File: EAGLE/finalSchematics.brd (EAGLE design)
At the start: 100 x 80 mm, 8 parts, among them IC1 STM32F103RBT, Q1 8MHz 131-220

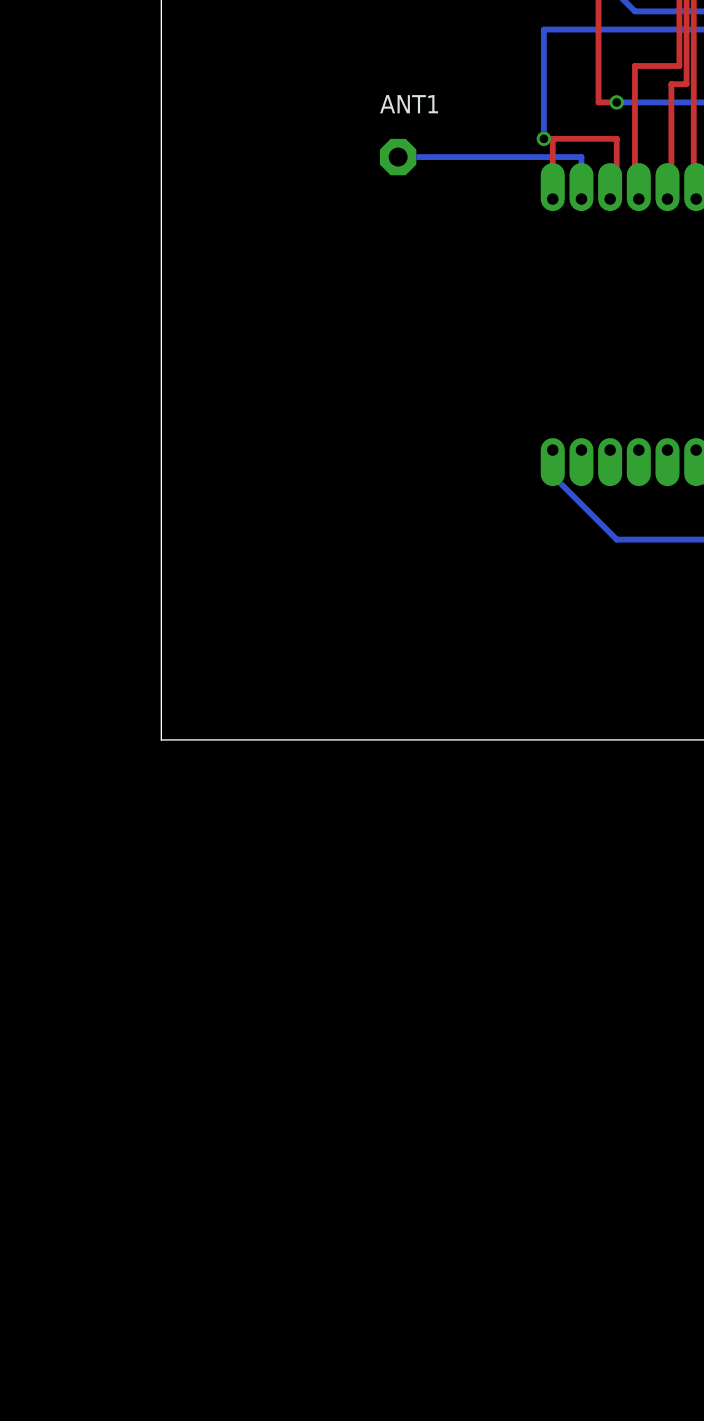
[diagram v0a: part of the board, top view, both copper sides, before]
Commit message: Eagle file ready for meeting with Vojta S.
Missing GPS module footer. Our module is L70 and only L80 library was
found. Will have to resolve later by creating a library at Mucirna.

Repositories folder updated with new documentation
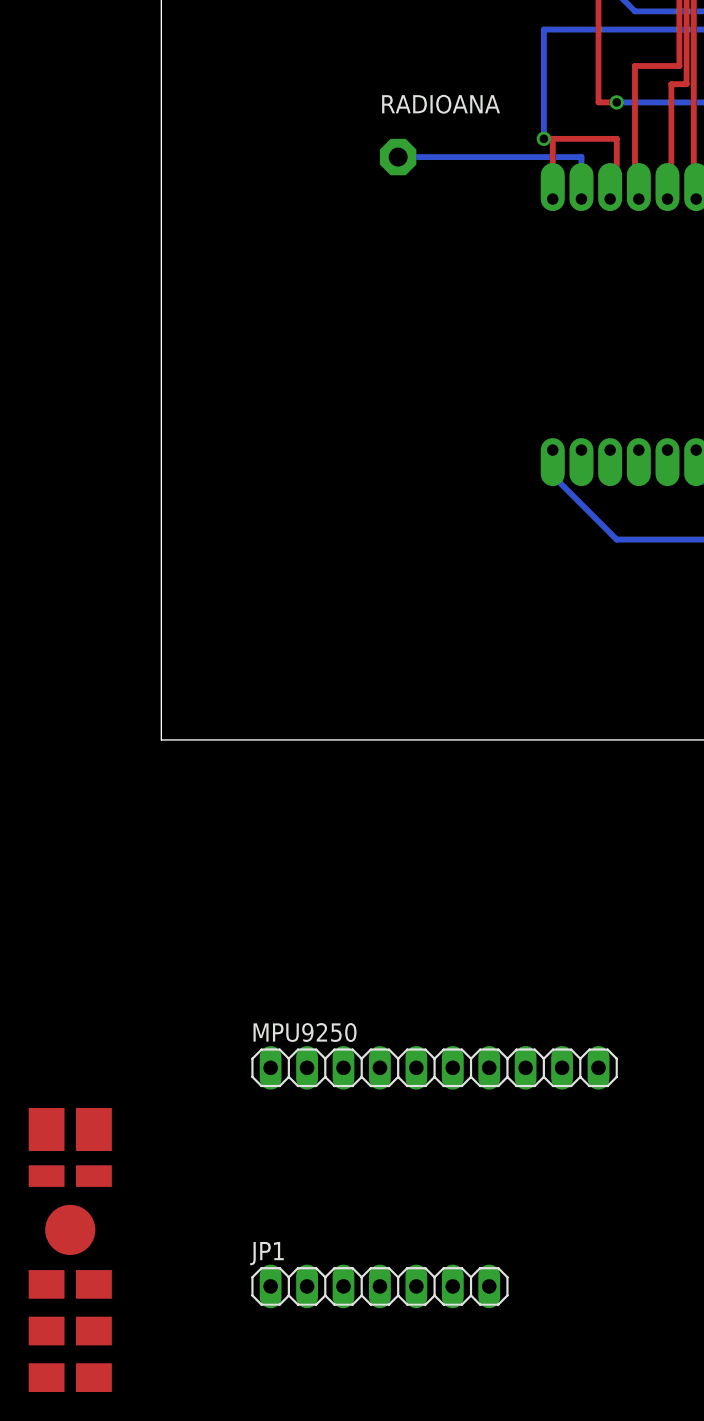
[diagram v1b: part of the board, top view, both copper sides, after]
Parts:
- added GPSANA: ANT-NSG4712-6, roundsolutions:ANT-NSG4712-6
- added JP1: (no value), pinhead:1X07
- added MPU9250: (no value), pinhead:1X10
- renumbered ANT1 to RADIOANA, BPM180 to BME280
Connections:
- new net ADO: MPU9250.4
- new net CD1: JP1.7
- new net CS: JP1.1
- new net DI: JP1.2
- new net DO: JP1.6
- new net ECL: MPU9250.5
- new net EDA: MPU9250.6
- new net FSYNC: MPU9250.1
- new net INT: MPU9250.3
- new net NCS: MPU9250.2
- new net SCK: JP1.4
- new net SCL: MPU9250.8
- new net SDA: MPU9250.7
- new net VCC: JP1.3, MPU9250.10
- net GND: now also JP1.5, MPU9250.9
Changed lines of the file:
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@@
 <layers>
 <layer number="1" name="Top" color="4" fill="1" visible="yes" active="yes"/>
+<layer number="2" name="Route2" color="1" fill="3" visible="no" active="no"/>
+<layer number="3" name="Route3" color="4" fill="3" visible="no" active="no"/>
+<layer number="4" name="Route4" color="1" fill="4" visible="no" active="no"/>
+<layer number="5" name="Route5" color="4" fill="4" visible="no" active="no"/>
+<layer number="6" name="Route6" color="1" fill="8" visible="no" active="no"/>
+<layer number="7" name="Route7" color="4" fill="8" visible="no" active="no"/>
+<layer number="8" name="Route8" color="1" fill="2" visible="no" active="no"/>
+<layer number="9" name="Route9" color="4" fill="2" visible="no" active="no"/>
+<layer number="10" name="Route10" color="1" fill="7" visible="no" active="no"/>
+<layer number="11" name="Route11" color="4" fill="7" visible="no" active="no"/>
+<layer number="12" name="Route12" color="1" fill="5" visible="no" active="no"/>
+<layer number="13" name="Route13" color="4" fill="5" visible="no" active="no"/>
+<layer number="14" name="Route14" color="1" fill="6" visible="no" active="no"/>
+<layer number="15" name="Route15" color="4" fill="6" visible="no" active="no"/>
 <layer number="16" name="Bottom" color="1" fill="1" visible="yes" active="yes"/>
 <layer number="17" name="Pads" color="2" fill="1" visible="yes" active="yes"/>
@@
 </autorouter>
 <elements>
-<element name="ANT1" library="discrete" package="PAD-01" value="" x="16.51" y="40.64"/>
+<element name="RADIOANA" library="discrete" package="PAD-01" value="" x="16.51" y="40.64"/>
 <element name="C1" library="rcl" package="C0805" value="4.7p 906-099" x="54.61" y="69.85" rot="R180"/>
 <element name="C2" library="rcl" package="C0805" value="4.7p 906-099" x="39.37" y="76.2" rot="R180"/>
@@
 <element name="R1" library="rcl" package="R0805" value="10k 901-655" x="50.8" y="59.69" rot="R180"/>
 <element name="U$1" library="RFM69mod" package="20X16BOARD" value="RFM69" x="34.29" y="29.21" rot="MR90"/>
-<element name="BPM180" library="pinhead" package="1X05/90" value="" x="76.2" y="62.23" rot="MR90"/>
+<element name="BME280" library="pinhead" package="1X05/90" value="" x="76.2" y="62.23" rot="MR90"/>
+<element name="MPU9250" library="pinhead" package="1X10" value="" x="19.05" y="-22.86"/>
+<element name="JP1" library="pinhead" package="1X07" value="" x="15.24" y="-38.1"/>
+<element name="GPSANA" library="roundsolutions" package="ANT-NSG4712-6" value="ANT-NSG4712-6" x="-6.35" y="-35.56"/>
 </elements>
 <signals>
@@
 <wire x1="26.67" y1="49.53" x2="26.67" y2="41.91" width="0.4064" layer="16"/>
 <via x="26.67" y="41.91" extent="1-16" drill="0.6"/>
-<contactref element="BPM180" pad="3"/>
+<contactref element="BME280" pad="3"/>
 <via x="52.07" y="49.53" extent="1-16" drill="0.6" shape="square"/>
 <wire x1="52.07" y1="58.42" x2="51.75" y2="59.69" width="0.4064" layer="1"/>
@@
 <wire x1="40.32" y1="76.2" x2="52.07" y2="76.2" width="0.4064" layer="1"/>
 <wire x1="52.07" y1="76.2" x2="58.42" y2="69.85" width="0.4064" layer="1"/>
+<contactref element="MPU9250" pad="9"/>
+<contactref element="JP1" pad="5"/>
+<wire x1="27.94" y1="-22.86" x2="27.29" y2="37.71" width="0" layer="19" extent="1-1"/>
+<wire x1="17.78" y1="-38.1" x2="27.94" y2="-22.86" width="0" layer="19" extent="1-1"/>
 </signal>
 <signal name="NC">
@@
 <signal name="N$3">
 <contactref element="U$1" pad="ANA"/>
-<contactref element="ANT1" pad="1"/>
+<contactref element="RADIOANA" pad="1"/>
 <wire x1="16.51" y1="40.64" x2="29.29" y2="40.64" width="0.4064" layer="16"/>
 <wire x1="29.29" y1="40.64" x2="29.29" y2="37.71" width="0.4064" layer="16"/>
@@
 <signal name="+3V3">
 <contactref element="U$1" pad="3.3V"/>
-<contactref element="BPM180" pad="2"/>
+<contactref element="BME280" pad="2"/>
 <wire x1="72.39" y1="59.69" x2="66.04" y2="59.69" width="0.4064" layer="16"/>
 <wire x1="66.04" y1="59.69" x2="58.42" y2="52.07" width="0.4064" layer="16"/>
@@
 <signal name="SCL_BPM180">
 <contactref element="IC1" pad="61"/>
-<contactref element="BPM180" pad="4"/>
+<contactref element="BME280" pad="4"/>
 <wire x1="45.12" y1="61.94" x2="53.05" y2="61.94" width="0.4064" layer="1"/>
 <wire x1="53.05" y1="61.94" x2="53.34" y2="62.23" width="0.4064" layer="1"/>
@@
 <signal name="SDA_BPM180">
 <contactref element="IC1" pad="62"/>
-<contactref element="BPM180" pad="5"/>
+<contactref element="BME280" pad="5"/>
 <wire x1="45.12" y1="62.44" x2="48.47" y2="62.44" width="0.4064" layer="1"/>
 <wire x1="48.47" y1="62.44" x2="49.53" y2="63.5" width="0.4064" layer="1"/>
@@
 <wire x1="53.34" y1="67.31" x2="72.39" y2="67.31" width="0.4064" layer="16"/>
 </signal>
+<signal name="VCC">
+<contactref element="MPU9250" pad="10"/>
+<contactref element="JP1" pad="3"/>
+<wire x1="30.48" y1="-22.86" x2="12.7" y2="-38.1" width="0" layer="19" extent="1-1"/>
+</signal>
+<signal name="SCL">
+<contactref element="MPU9250" pad="8"/>
+</signal>
+<signal name="SDA">
+<contactref element="MPU9250" pad="7"/>
+</signal>
+<signal name="EDA">
+<contactref element="MPU9250" pad="6"/>
+</signal>
+<signal name="ECL">
+<contactref element="MPU9250" pad="5"/>
+</signal>
+<signal name="ADO">
+<contactref element="MPU9250" pad="4"/>
+</signal>
+<signal name="INT">
+<contactref element="MPU9250" pad="3"/>
+</signal>
+<signal name="NCS">
+<contactref element="MPU9250" pad="2"/>
+</signal>
+<signal name="FSYNC">
+<contactref element="MPU9250" pad="1"/>
+</signal>
+<signal name="CS">
+<contactref element="JP1" pad="1"/>
+</signal>
+<signal name="DI">
+<contactref element="JP1" pad="2"/>
+</signal>
+<signal name="SCK">
+<contactref element="JP1" pad="4"/>
+</signal>
+<signal name="DO">
+<contactref element="JP1" pad="6"/>
+</signal>
+<signal name="CD1">
+<contactref element="JP1" pad="7"/>
+</signal>
 </signals>

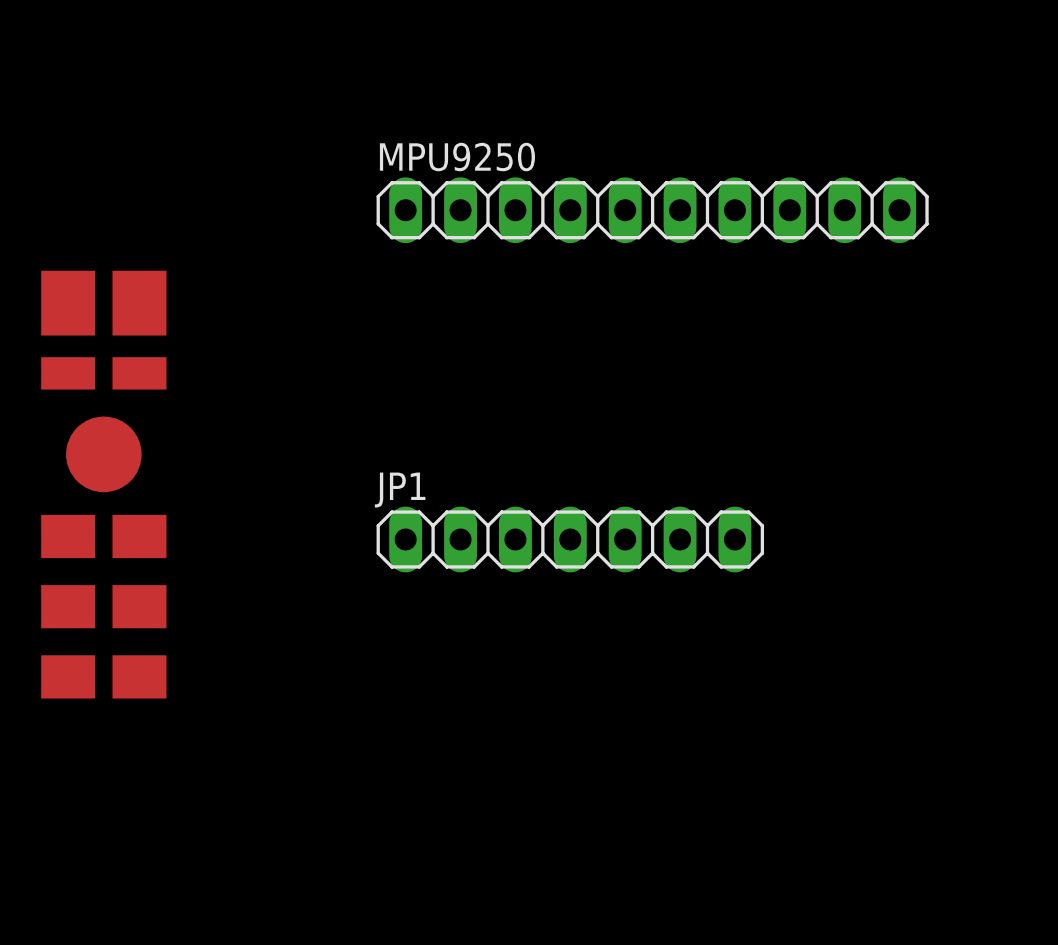
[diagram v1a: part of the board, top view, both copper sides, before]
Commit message: SDfixed, Gyro fixed
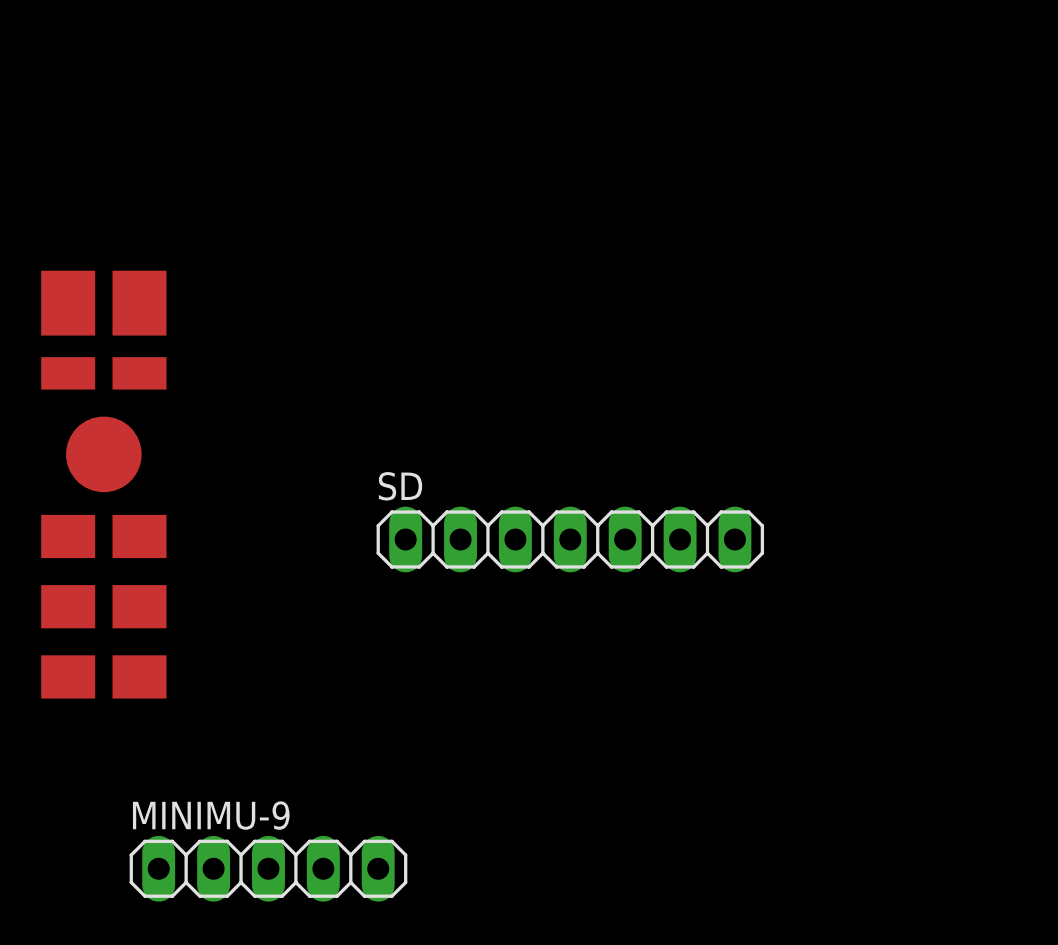
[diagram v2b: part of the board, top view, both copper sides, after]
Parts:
- removed MPU9250: (no value), pinhead:1X10
- added MINIMU-9: (no value), pinhead:1X05
- renumbered JP1 to SD
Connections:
- removed net ADO: MPU9250.4
- removed net ECL: MPU9250.5
- removed net EDA: MPU9250.6
- removed net FSYNC: MPU9250.1
- removed net INT: MPU9250.3
- removed net NCS: MPU9250.2
- new net VIN: MINIMU-9.2
- net GND: now also MINIMU-9.3; no longer MPU9250.9
- net SCL: now also MINIMU-9.5; no longer MPU9250.8
- net SDA: now also MINIMU-9.4; no longer MPU9250.7
- net VCC: no longer MPU9250.10
- net VDD: now also MINIMU-9.1
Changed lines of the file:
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@@
 <element name="U$1" library="RFM69mod" package="20X16BOARD" value="RFM69" x="34.29" y="29.21" rot="MR90"/>
 <element name="BME280" library="pinhead" package="1X05/90" value="" x="76.2" y="62.23" rot="MR90"/>
-<element name="MPU9250" library="pinhead" package="1X10" value="" x="19.05" y="-22.86"/>
-<element name="JP1" library="pinhead" package="1X07" value="" x="15.24" y="-38.1"/>
+<element name="SD" library="pinhead" package="1X07" value="" x="15.24" y="-38.1"/>
 <element name="GPSANA" library="roundsolutions" package="ANT-NSG4712-6" value="ANT-NSG4712-6" x="-6.35" y="-35.56"/>
+<element name="MINIMU-9" library="pinhead" package="1X05" value="" x="1.27" y="-53.34"/>
 </elements>
 <signals>
@@
 <wire x1="33.08" y1="55.94" x2="31.75" y2="54.61" width="0.4064" layer="1"/>
 <via x="31.75" y="54.61" extent="1-16" drill="0.6"/>
+<contactref element="MINIMU-9" pad="1"/>
+<wire x1="-3.81" y1="-53.34" x2="33.02" y2="50.8" width="0" layer="19" extent="16-16"/>
 </signal>
 <signal name="VSS">
@@
 <wire x1="40.32" y1="76.2" x2="52.07" y2="76.2" width="0.4064" layer="1"/>
 <wire x1="52.07" y1="76.2" x2="58.42" y2="69.85" width="0.4064" layer="1"/>
-<contactref element="MPU9250" pad="9"/>
-<contactref element="JP1" pad="5"/>
-<wire x1="27.94" y1="-22.86" x2="27.29" y2="37.71" width="0" layer="19" extent="1-1"/>
-<wire x1="17.78" y1="-38.1" x2="27.94" y2="-22.86" width="0" layer="19" extent="1-1"/>
+<contactref element="SD" pad="5"/>
+<contactref element="MINIMU-9" pad="3"/>
+<wire x1="17.78" y1="-38.1" x2="27.29" y2="37.71" width="0" layer="19" extent="1-1"/>
+<wire x1="1.27" y1="-53.34" x2="17.78" y2="-38.1" width="0" layer="19" extent="1-1"/>
 </signal>
 <signal name="NC">
@@
 </signal>
 <signal name="VCC">
-<contactref element="MPU9250" pad="10"/>
-<contactref element="JP1" pad="3"/>
-<wire x1="30.48" y1="-22.86" x2="12.7" y2="-38.1" width="0" layer="19" extent="1-1"/>
+<contactref element="SD" pad="3"/>
+</signal>
+<signal name="CS">
+<contactref element="SD" pad="1"/>
+</signal>
+<signal name="DI">
+<contactref element="SD" pad="2"/>
+</signal>
+<signal name="SCK">
+<contactref element="SD" pad="4"/>
+</signal>
+<signal name="DO">
+<contactref element="SD" pad="6"/>
+</signal>
+<signal name="CD1">
+<contactref element="SD" pad="7"/>
 </signal>
 <signal name="SCL">
-<contactref element="MPU9250" pad="8"/>
+<contactref element="MINIMU-9" pad="5"/>
 </signal>
 <signal name="SDA">
-<contactref element="MPU9250" pad="7"/>
-</signal>
-<signal name="EDA">
-<contactref element="MPU9250" pad="6"/>
-</signal>
-<signal name="ECL">
-<contactref element="MPU9250" pad="5"/>
-</signal>
-<signal name="ADO">
-<contactref element="MPU9250" pad="4"/>
-</signal>
-<signal name="INT">
-<contactref element="MPU9250" pad="3"/>
-</signal>
-<signal name="NCS">
-<contactref element="MPU9250" pad="2"/>
-</signal>
-<signal name="FSYNC">
-<contactref element="MPU9250" pad="1"/>
-</signal>
-<signal name="CS">
-<contactref element="JP1" pad="1"/>
-</signal>
-<signal name="DI">
-<contactref element="JP1" pad="2"/>
-</signal>
-<signal name="SCK">
-<contactref element="JP1" pad="4"/>
-</signal>
-<signal name="DO">
-<contactref element="JP1" pad="6"/>
-</signal>
-<signal name="CD1">
-<contactref element="JP1" pad="7"/>
+<contactref element="MINIMU-9" pad="4"/>
+</signal>
+<signal name="VIN">
+<contactref element="MINIMU-9" pad="2"/>
 </signal>
 </signals>
